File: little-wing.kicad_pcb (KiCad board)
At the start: 2 copper layers, 119.8 x 94.8 mm, 72 parts, among them IC1 AP7335-WG-7, J1 nice!view, J2 Battery, J3 trackball, J4 trackball, SW1 Power, SW2 Reset, U1 nice!nano v2, U2 PMW3610

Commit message: Clearing out all the wiring
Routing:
- net GND: track 763.2 -> 0.00 mm, vias 23 -> 0
- net VCC: track 681.9 -> 0.00 mm, vias 31 -> 0
- net Row 0: track 438.6 -> 0.00 mm, vias 26 -> 0
- net Row 1: track 391.8 -> 0.00 mm, vias 22 -> 0
- net Row 2: track 281.6 -> 0.00 mm, vias 9 -> 0
- net Col 0: track 230.3 -> 0.00 mm, vias 5 -> 0
- net Col 1: track 203.0 -> 0.00 mm, vias 5 -> 0
- net RGB: track 199.4 -> 0.00 mm, vias 1 -> 0
- net Col 2: track 178.5 -> 0.00 mm, vias 5 -> 0
- net Col 3: track 166.4 -> 0.00 mm, vias 5 -> 0
- net Col 4: track 142.0 -> 0.00 mm, vias 5 -> 0
- net Net-(D31-DIN): track 124.0 -> 0.00 mm, vias 2 -> 0
- net Net-(D19-DIN): track 121.5 -> 0.00 mm, vias 4 -> 0
- net Net-(D22-DIN): track 111.9 -> 0.00 mm, vias 2 -> 0
- net Net-(D28-DIN): track 107.2 -> 0.00 mm, vias 2 -> 0
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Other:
- copper layers 2 -> 4

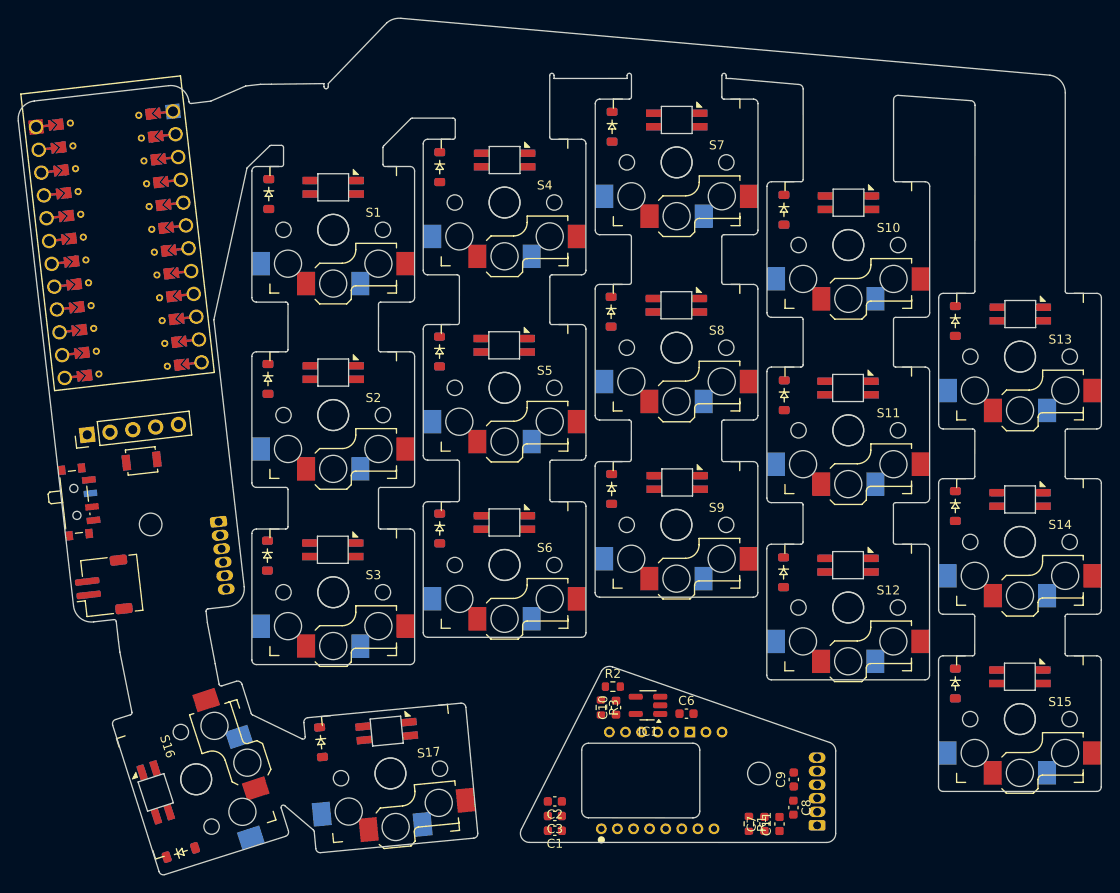
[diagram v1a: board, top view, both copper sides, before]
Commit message: Rewiring one column in the 4 stack configuration
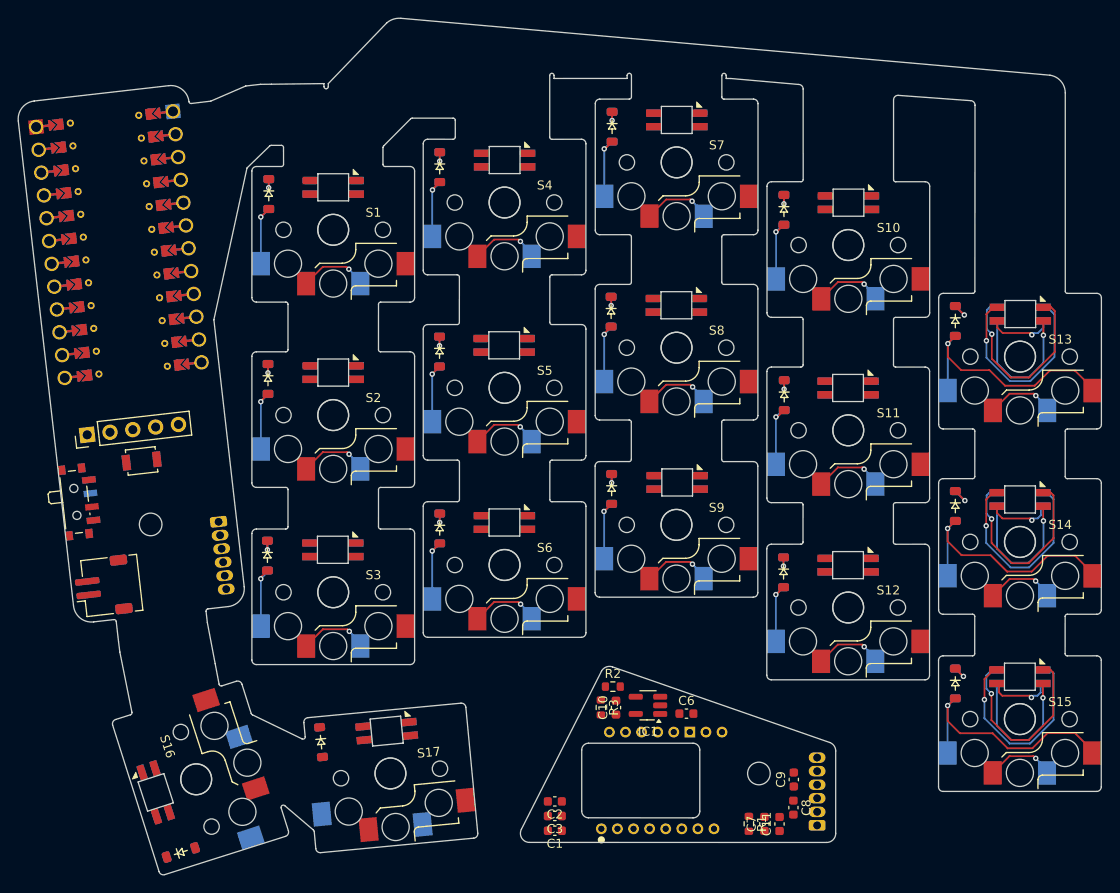
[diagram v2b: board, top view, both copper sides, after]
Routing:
- net GND: track 0.00 -> 130.8 mm, vias 0 -> 3
- net VCC: track 0.00 -> 98.4 mm, vias 0 -> 3
- net Col 0: track 0.00 -> 98.3 mm, vias 0 -> 3
- net RGB: track 0.00 -> 82.0 mm, vias 0 -> 1
- net Row 0: track 0.00 -> 75.8 mm, vias 0 -> 5
- net Net-(D32-DIN): track 0.00 -> 61.8 mm, vias 0 -> 2
- net Net-(D33-DIN): track 0.00 -> 60.8 mm, vias 0 -> 2
- net Row 1: track 0.00 -> 55.6 mm, vias 0 -> 5
- net Net-(D31-DIN): track 0.00 -> 48.7 mm, vias 0 -> 1
- net Row 2: track 0.00 -> 34.3 mm, vias 0 -> 5
- net Net-(D15-A): track 0.00 -> 28.3 mm, vias 0 -> 1
- net Net-(D14-A): track 0.00 -> 28.3 mm, vias 0 -> 1
- net Net-(D13-A): track 0.00 -> 28.1 mm, vias 0 -> 1
- net Col 1: track 0.00 -> 23.3 mm, vias 0 -> 3
- net Col 3: track 0.00 -> 23.3 mm, vias 0 -> 3
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
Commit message: Wiring up all the main column pads
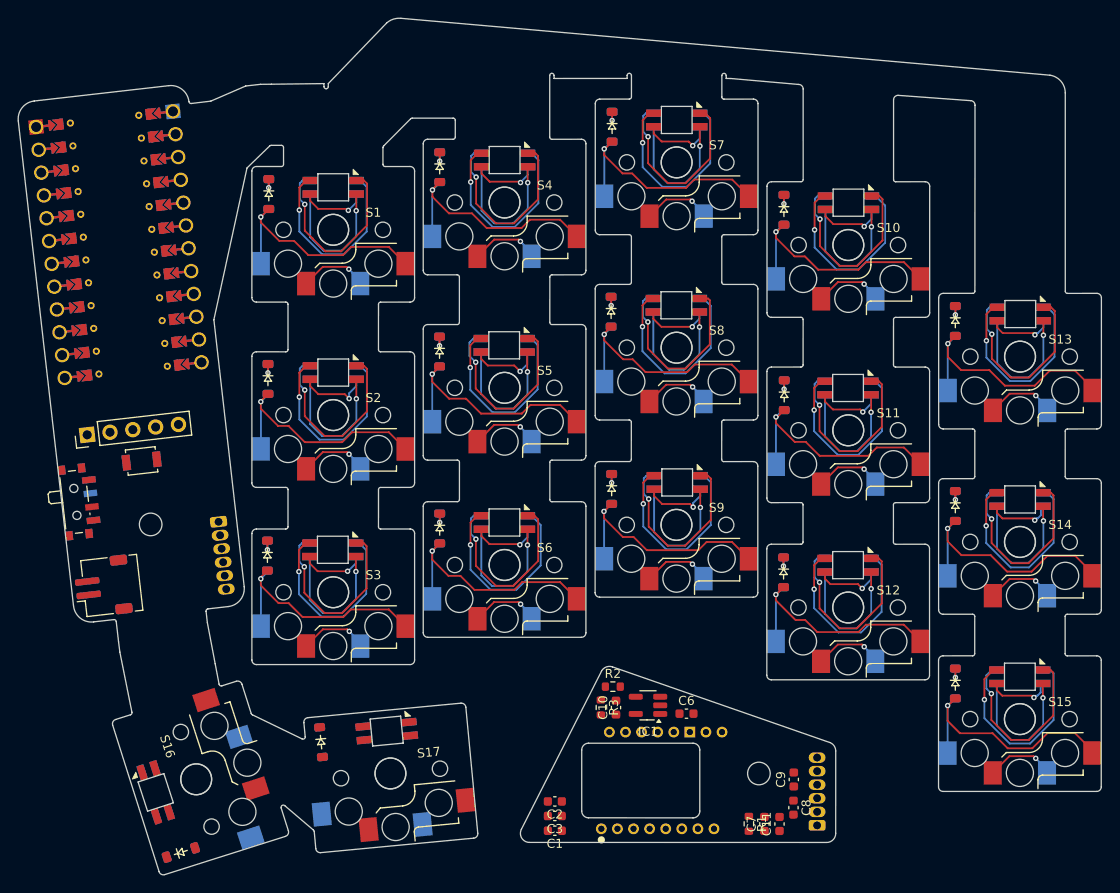
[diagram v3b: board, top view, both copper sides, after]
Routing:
- net GND: track 130.8 -> 391.0 mm, vias 3 -> 15
- net VCC: track 98.4 -> 191.7 mm, vias 3 -> 15
- net Net-(D24-DIN): track 0.00 -> 38.7 mm, vias 0 -> 2
- net Net-(D25-DIN): track 0.00 -> 38.5 mm, vias 0 -> 2
- net Net-(D26-DIN): track 0.00 -> 38.3 mm, vias 0 -> 2
- net Net-(D28-DIN): track 0.00 -> 38.3 mm, vias 0 -> 2
- net Net-(D20-DIN): track 0.00 -> 38.3 mm, vias 0 -> 2
- net Net-(D22-DIN): track 0.00 -> 38.2 mm, vias 0 -> 2
- net Net-(D23-DIN): track 0.00 -> 38.2 mm, vias 0 -> 2
- net Net-(D21-DIN): track 0.00 -> 38.2 mm, vias 0 -> 2
- net Net-(D30-DIN): track 0.00 -> 38.2 mm, vias 0 -> 2
- net Net-(D27-DIN): track 0.00 -> 38.1 mm, vias 0 -> 2
- net Net-(D29-DIN): track 0.00 -> 38.0 mm, vias 0 -> 2
- net Net-(D19-DIN): track 0.00 -> 22.3 mm, vias 0 -> 1
- net Net-(D2-A): track 7.62 -> 27.2 mm
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
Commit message: Wiring up the main columns
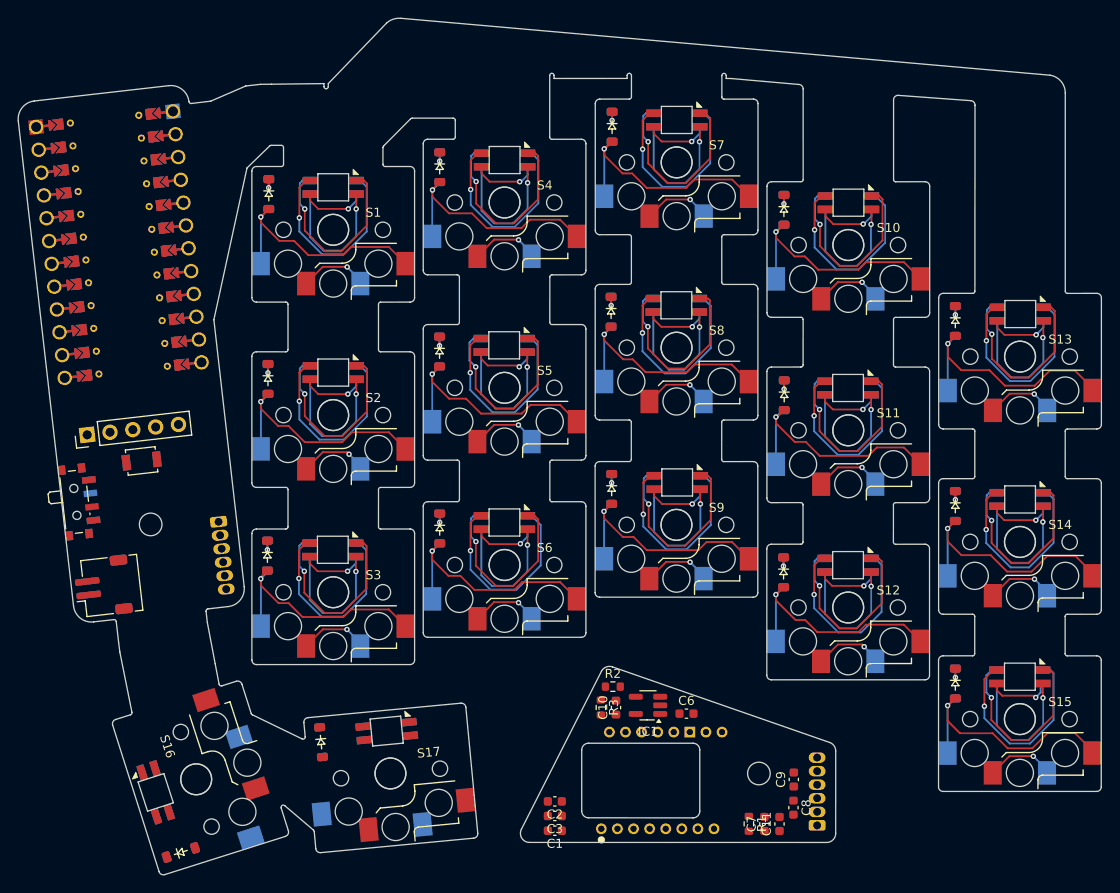
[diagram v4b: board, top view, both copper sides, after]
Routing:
- net VCC: track 191.7 -> 447.3 mm
- net GND: track 391.0 -> 600.2 mm
- net Row 0: track 76.2 -> 284.9 mm
- net Row 1: track 55.6 -> 181.7 mm
- net Net-(D28-DIN): track 38.3 -> 116.7 mm
- net Net-(D25-DIN): track 38.5 -> 111.7 mm
- net Net-(D22-DIN): track 38.2 -> 107.6 mm
- net Net-(D31-DIN): track 64.5 -> 132.0 mm
- net Col 1: track 23.3 -> 87.5 mm
- net Col 2: track 23.3 -> 81.6 mm
- net Col 3: track 23.3 -> 81.5 mm
- net Col 4: track 23.2 -> 80.9 mm
- net Row 2: track 34.3 -> 72.5 mm
- net Net-(D20-DIN): track 38.3 -> 62.2 mm
- net Net-(D29-DIN): track 38.0 -> 61.7 mm
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
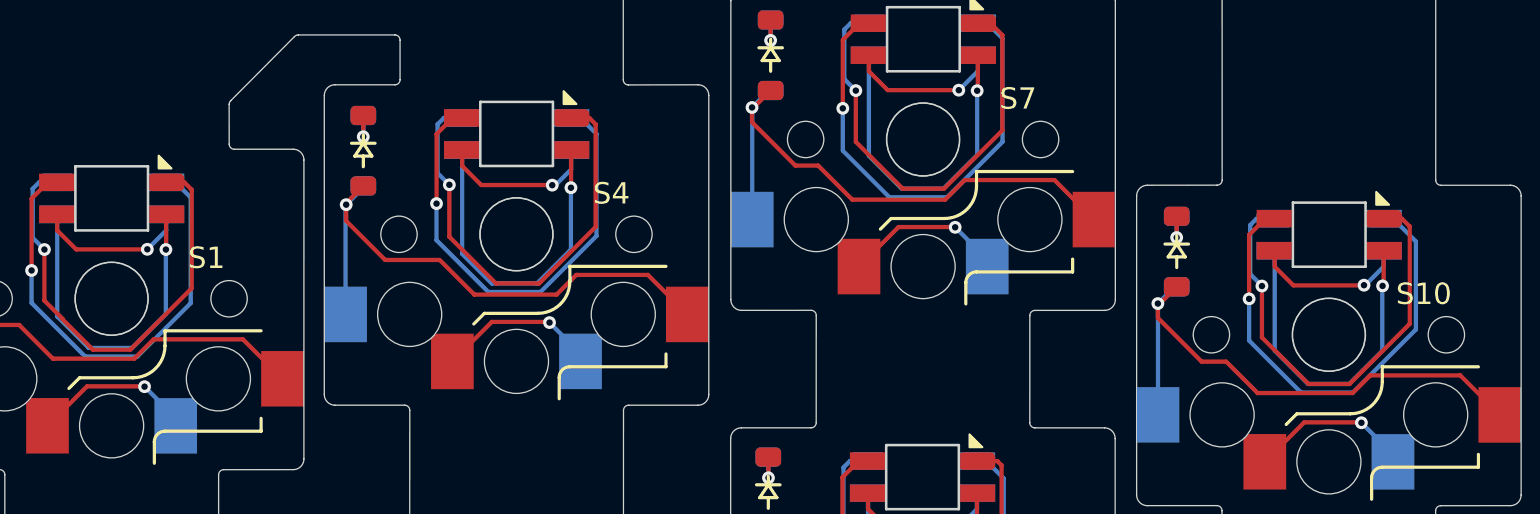
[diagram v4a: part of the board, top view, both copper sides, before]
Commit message: The first pass wiring together the columns
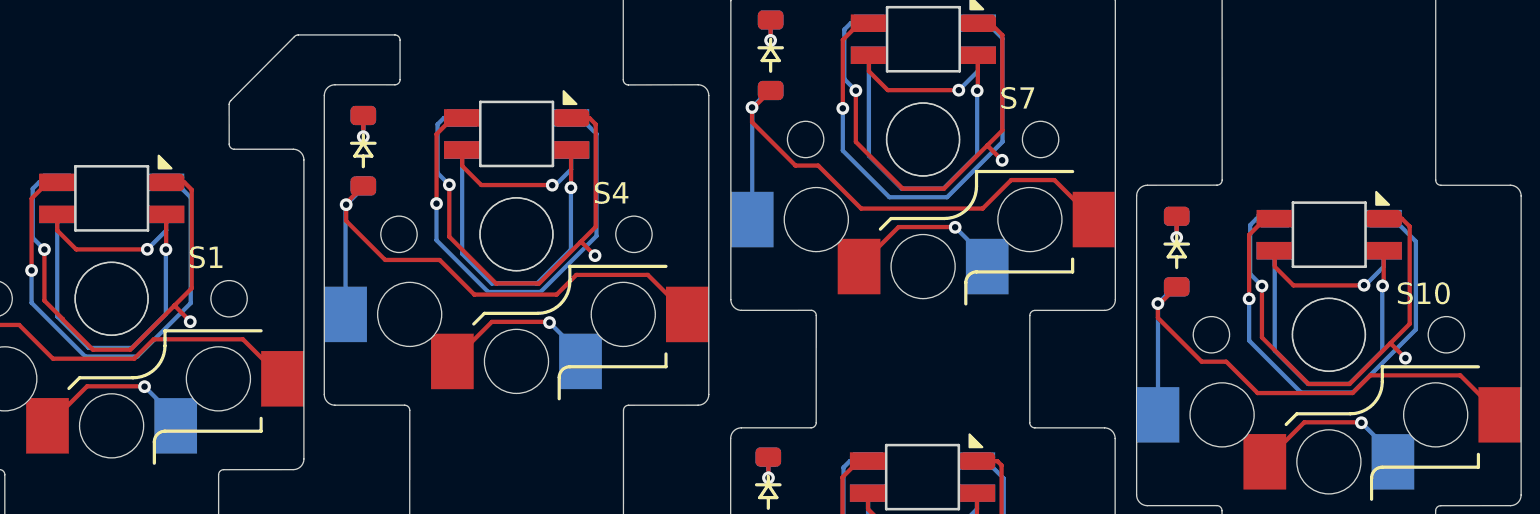
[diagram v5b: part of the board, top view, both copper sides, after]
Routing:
- net Row 0: track 284.9 -> 396.5 mm
- net VCC: track 447.3 -> 556.3 mm
- net GND: track 600.2 -> 706.9 mm, vias 15 -> 19
- net Row 1: track 181.7 -> 283.3 mm
- net RGB: track 81.3 -> 175.1 mm
- net Col 0: track 98.4 -> 190.4 mm
- net Row 2: track 72.5 -> 162.6 mm
- net Col 1: track 87.5 -> 163.6 mm
- net Col 2: track 81.6 -> 136.0 mm
- net Col 3: track 81.5 -> 121.5 mm
- net Col 4: track 80.9 -> 94.0 mm
- net Net-(D28-DIN): track 116.7 -> 114.8 mm
- net Net-(D22-DIN): track 107.6 -> 106.6 mm
- net Net-(D19-DIN): track 33.4 -> 32.5 mm
- net Net-(D25-DIN): track 111.7 -> 112.7 mm
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
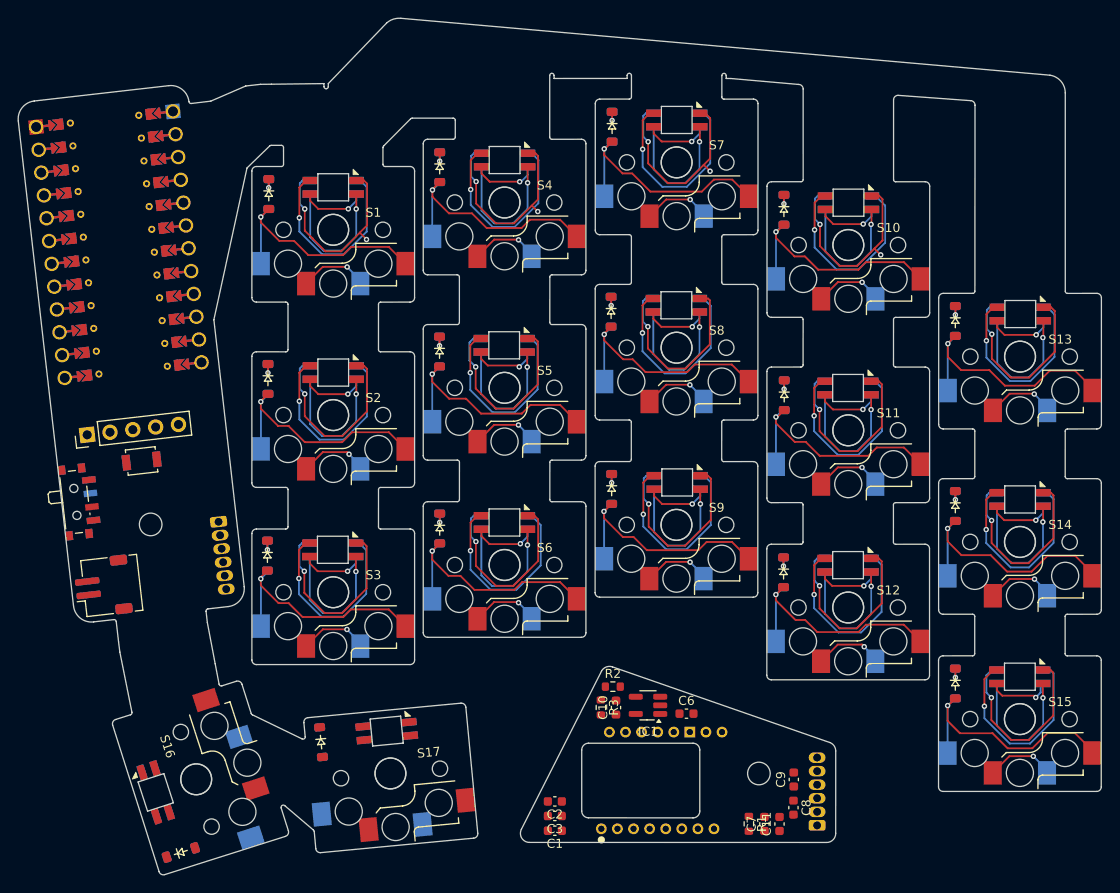
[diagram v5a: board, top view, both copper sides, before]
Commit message: Completing the columns wiring
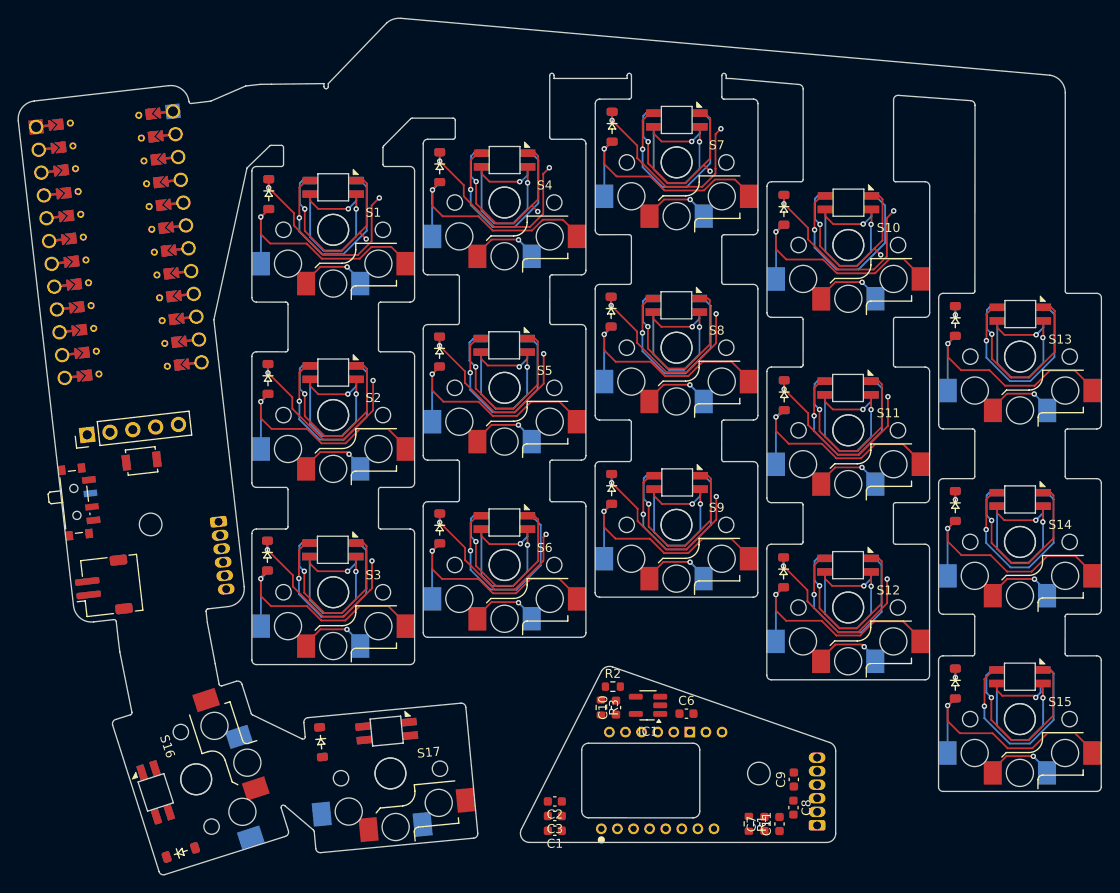
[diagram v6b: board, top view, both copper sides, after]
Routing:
- net Row 0: track 396.5 -> 646.0 mm, vias 5 -> 9
- net Row 1: track 283.3 -> 447.6 mm, vias 5 -> 9
- net Row 2: track 162.6 -> 244.0 mm, vias 5 -> 9
- net Net-(D10-A): track 26.9 -> 28.4 mm
- net Net-(D3-A): track 27.0 -> 28.5 mm
- net Net-(D12-A): track 26.8 -> 28.2 mm
- net Net-(D8-A): track 26.8 -> 28.2 mm
- net Net-(D6-A): track 27.1 -> 28.6 mm
- net Net-(D9-A): track 27.0 -> 28.3 mm
- net Net-(D5-A): track 27.1 -> 28.4 mm
- net Net-(D1-A): track 26.9 -> 28.2 mm
- net Net-(D11-A): track 27.0 -> 28.2 mm
- net Net-(D2-A): track 27.2 -> 28.4 mm
- net Net-(D4-A): track 26.9 -> 27.9 mm
- net Net-(D7-A): track 27.3 -> 28.0 mm
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
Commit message: Cleaning up the columns wiring
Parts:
- turned S14 to -1.77636e-15 degrees
- turned S10 to -1.77636e-15 degrees
- turned D31 to -1.77636e-15 degrees
- turned D27 to -1.77636e-15 degrees
- turned D29 to -1.77636e-15 degrees
- turned D33 to -1.77636e-15 degrees
- turned S3 to -1.77636e-15 degrees
- turned S1 to -1.77636e-15 degrees
- turned S7 to -1.77636e-15 degrees
- turned D21 to -1.77636e-15 degrees
- turned D23 to -1.77636e-15 degrees
- turned S4 to -1.77636e-15 degrees
- turned S6 to -1.77636e-15 degrees
- turned D30 to -1.77636e-15 degrees
- turned D26 to -1.77636e-15 degrees
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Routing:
- net VCC: track 556.5 -> 550.0 mm
- net GND: track 706.8 -> 712.6 mm
- net Net-(D19-DIN): track 32.4 -> 37.5 mm
- net Col 0: track 190.9 -> 195.1 mm
- net Row 2: track 244.0 -> 247.5 mm
- net Row 1: track 447.6 -> 450.9 mm
- net Row 0: track 646.0 -> 648.8 mm
- net Col 3: track 122.0 -> 124.5 mm
- net Col 2: track 136.4 -> 138.7 mm
- net Col 1: track 164.1 -> 165.9 mm
- net RGB: track 175.1 -> 176.4 mm
- net Col 4: track 94.5 -> 95.6 mm
- net Net-(D22-DIN): track 106.6 -> 107.7 mm

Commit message: Cleaning up the main columns exit wiring
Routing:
- net GND: track 712.6 -> 716.6 mm
- net RGB: track 176.4 -> 180.1 mm
- net Row 1: track 450.9 -> 453.6 mm
- net Net-(D19-DIN): track 37.5 -> 39.5 mm
- net Col 4: track 95.6 -> 97.4 mm
- net Col 2: track 138.7 -> 140.0 mm
- net Row 0: track 648.8 -> 649.9 mm
- net VCC: track 550.0 -> 551.1 mm
- net Col 3: track 124.5 -> 125.6 mm
- net Col 0: track 195.1 -> 196.0 mm
- net Col 1: track 165.9 -> 166.7 mm
- net Row 2: track 247.5 -> 246.9 mm
